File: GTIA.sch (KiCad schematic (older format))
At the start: 0 parts

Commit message: GTIA
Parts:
- added C111: 820pF, Atari:C_Axial_L5.1mm_D2.5mm_P12.50mm_Horizontal, symbol Device:C
- added C206, C59: 22pF, Atari:C_Axial_L5.1mm_D2.5mm_P12.50mm_Horizontal, symbol Device:C
- added C42, C48, C51, C58, C61: 100nF, Atari:C_Axial_L5.1mm_D2.5mm_P12.50mm_Horizontal, symbol Device:C
- added C44: 68pF, Atari:C_Axial_L5.1mm_D2.5mm_P12.50mm_Horizontal, symbol Device:C
- added C45: 220pF, Atari:C_Axial_L5.1mm_D2.5mm_P12.50mm_Horizontal, symbol Device:C
- added C46, C47, C96, C97: 1nF, Atari:C_Axial_L5.1mm_D2.5mm_P12.50mm_Horizontal, symbol Device:C
- added C50: 10uF, Capacitor_THT:CP_Radial_D8.0mm_P2.50mm, symbol Device:CP
- added C60: 560pF, Atari:C_Axial_L5.1mm_D2.5mm_P12.50mm_Horizontal, symbol Device:C
- added D2, D3, D4: 1N4148, Diode_THT:D_DO-35_SOD27_P7.62mm_Horizontal, symbol Diode:1N4148
- added FB31, FB9: Ferrite_Bead, Atari:L_Axial_L7.0mm_D3.3mm_P12.50mm_Horizontal_Fastron_MICC, symbol Device:Ferrite_Bead
- added L23, L30, L6, L66: 100uH, symbol Device:L
- added L37: Bead or 470R, symbol Device:L
- added L5: 820uH, symbol Device:L
- added L8: 1,5uH, symbol Device:L
- added Q1, Q2, Q3, Q6: 2N3904, Package_TO_SOT_THT:TO-92, symbol Transistor_BJT:2N3904
- added R116: 51, Atari:R_Axial_DIN0207_L3.6mm_D2.2mm_P10.16mm_Horizontal, symbol Device:R
- added R132, R133: 220, Atari:R_Axial_DIN0207_L3.6mm_D2.2mm_P10.16mm_Horizontal, symbol Device:R
- added R134, R135, R136, R71: 470, Atari:R_Axial_DIN0207_L3.6mm_D2.2mm_P10.16mm_Horizontal, symbol Device:R
- added R201, R69: 6k8, Atari:R_Axial_DIN0207_L3.6mm_D2.2mm_P10.16mm_Horizontal, symbol Device:R
- added R202: 180, Atari:R_Axial_DIN0207_L3.6mm_D2.2mm_P10.16mm_Horizontal, symbol Device:R
- added R204: 47, Atari:R_Axial_DIN0207_L3.6mm_D2.2mm_P10.16mm_Horizontal, symbol Device:R
- added R205: 150, Atari:R_Axial_DIN0207_L3.6mm_D2.2mm_P10.16mm_Horizontal, symbol Device:R
- added R33: 3k3, Atari:R_Axial_DIN0207_L3.6mm_D2.2mm_P10.16mm_Horizontal, symbol Device:R
- added R35: 33k, Atari:R_Axial_DIN0207_L3.6mm_D2.2mm_P10.16mm_Horizontal, symbol Device:R
- added R36: 680, Atari:R_Axial_DIN0207_L3.6mm_D2.2mm_P10.16mm_Horizontal, symbol Device:R
- added R37, R41, R42, R43, R44, R45, R72: 1k, Atari:R_Axial_DIN0207_L3.6mm_D2.2mm_P10.16mm_Horizontal, symbol Device:R
- added R46: 1k6, Atari:R_Axial_DIN0207_L3.6mm_D2.2mm_P10.16mm_Horizontal, symbol Device:R
- added R47: 36k, Atari:R_Axial_DIN0207_L3.6mm_D2.2mm_P10.16mm_Horizontal, symbol Device:R
- added R48: 18k, Atari:R_Axial_DIN0207_L3.6mm_D2.2mm_P10.16mm_Horizontal, symbol Device:R
- added R49: 9k1, Atari:R_Axial_DIN0207_L3.6mm_D2.2mm_P10.16mm_Horizontal, symbol Device:R
- added R50, R73: 4k7, Atari:R_Axial_DIN0207_L3.6mm_D2.2mm_P10.16mm_Horizontal, symbol Device:R
- added R51: 750, Atari:R_Axial_DIN0207_L3.6mm_D2.2mm_P10.16mm_Horizontal, symbol Device:R
- added R52: 2k, Atari:R_Axial_DIN0207_L3.6mm_D2.2mm_P10.16mm_Horizontal, symbol Device:R
- added R53: 100, Atari:R_Axial_DIN0207_L3.6mm_D2.2mm_P10.16mm_Horizontal, symbol Device:R
- added R70: 10k, Atari:R_Axial_DIN0207_L3.6mm_D2.2mm_P10.16mm_Horizontal, symbol Device:R
- added RV38: 500k, Potentiometer_THT:Potentiometer_ACP_CA9-V10_Vertical_Hole, symbol Device:R_POT
- added U17: GTIA, Package_DIP:DIP-40_W15.24mm_Socket, symbol Atari:GTIA
- added U18: 74LS08, Package_DIP:DIP-14_W7.62mm_Socket, symbol 74xx:74LS08
- added U20: 4050, Package_DIP:DIP-16_W7.62mm_Socket, symbol 4xxx:4050
- added U21: 74LS74, Package_DIP:DIP-14_W7.62mm_Socket, symbol 74xx:74LS74
- added Y2: 4,43 MHz, Crystal:Crystal_HC18-U_Horizontal, symbol Device:Crystal
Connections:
- new net: R134.2, U17.12 (S0)
- new net: R135.2, U17.13 (S1)
- new net: R136.2, U17.14 (S2)
- new net: Q6.3 (C), R70.1, R72.2, U17.16 (PAL)
- new net: C48.2, RV38.2, U17.17 (CADJ)
- new net: L6.2, R33.2, R41.2, U17.21 (COLOR)
- new net: R44.2, U17.22 (LUM1), U20.11
- new net: R43.2, U17.23 (LUM2), U20.5
- new net: R42.2, U17.24 (LUM3), U20.3
- new net: U17.25 (CSYNC), U20.14
- new net: C206.2, L37.1, U17.28 (OSC), U21.3 (C)
- new net: R45.2, U17.31 (LUM0), U20.7
- new net: R132.2, U17.8 (T0), U18.12
- new net: R133.2, U17.9 (T1), U18.13
- new net: C44.1, Q1.2 (B), R35.2
- new net: C45.2, Q1.3 (C), R36.2
- new net: C45.1, D2.1 (K), D3.2 (A)
- new net: C46.2, D3.1 (K), R37.2
- new net: C47.2, R37.1, RV38.1
- new net: U21.2 (D), U21.6 (~Q)
- new net: U21.11 (C), U21.5 (Q)
- new net: U21.12 (D), U21.8 (~Q)
- new net: C59.1, C60.2, R73.2, U21.9 (Q)
- new net: C58.2, U21.7 (GND)
- new net: C59.2, Y2.1
- new net: C111.1, L8.1, R71.2, Y2.2
- new net: Q6.2 (B), R69.1, R70.2, R71.1
- new net: C111.2, C61.2, L8.2
- new net: R50.2, U20.2
- new net: R49.2, U20.4
- new net: R47.2, U20.6
- new net: R48.2, U20.12
- new net: D4.1 (K), U20.15
- new net: C50.1, C51.1, L5.1, R116.1, R46.1, U20.1 (VCC)
- new net: Q3.2 (B), R46.2, R47.1, R48.1, R49.1, R50.1, R51.1, R52.1
- new net: D4.2 (A), R51.2
- new net: Q3.1 (E), R204.2, R53.1
- new net: Q3.3 (C), R116.2
- new net: FB9.2, R204.1
- new net: L66.2, R33.1
- new net: Q2.2 (B), R201.1
- new net: L6.1, R201.2
- new net: Q2.1 (E), R202.2, R205.2
- new net: FB31.2, R205.1
- new net: C97.2, L30.2, R132.1
- new net: C96.2, L23.2, R133.1
- new net +5C: Q2.3 (C)
- new net +5VA: C42.1, C58.1, D2.2 (A), L5.2, R35.1, R36.1, R41.1, R42.1, R43.1, R44.1, R45.1, R72.1, R73.1, U17.27 (VCC), U21.1 (~R), U21.10 (~S), U21.13 (~R), U21.14 (VCC), U21.4 (~S)
- new net A0: U17.2 (A0)
- new net A1: U17.1 (A1)
- new net A2: U17.40 (A2)
- new net A3: U17.39 (A3)
- new net A4: U17.38 (A4)
- new net AN0: U17.18 (AN0)
- new net AN1: U17.19 (AN1)
- new net AN2: U17.20 (AN2)
- new net BELL: U17.15 (S3)
- new net CHROMA: FB31.1
- new net COLOR: L66.1
- new net D0: U17.7 (D0)
- new net D1: U17.6 (D1)
- new net D2: U17.5 (D2)
- new net D3: U17.4 (D3)
- new net D4: U17.37 (D4)
- new net D5: U17.36 (D5)
- new net D6: U17.35 (D6)
- new net D7: U17.34 (D7)
- new net FO0: U17.29 (FO0)
- new net GND: C206.1, C42.2, C46.1, C47.1, C48.1, C50.2, C51.2, C60.1, C61.1, C96.1, C97.1, Q1.1 (E), Q6.1 (E), R202.1, R52.2, R53.2, R69.2, RV38.3, U17.3 (VSS), U20.8 (VSS), U20.9
- new net GTIA: U17.32 (~CS)
- new net HALT: U17.26 (HALT)
- new net LP: U18.11
- new net MONO: FB9.1
- new net O1: C44.2
- new net O2: U17.30 (O2)
- new net OPTION: R136.1
- new net OSC: L37.2
- new net RD5: U17.11 (T3)
- new net RW: U17.33 (R/~W)
- new net SELECT: R135.1
- new net START: R134.1
- new net TRIG0: L30.1
- new net TRIG1: L23.1
- no-connect marks 0 -> 1
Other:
- note added: "When L=470R\nC206 is not mounted"

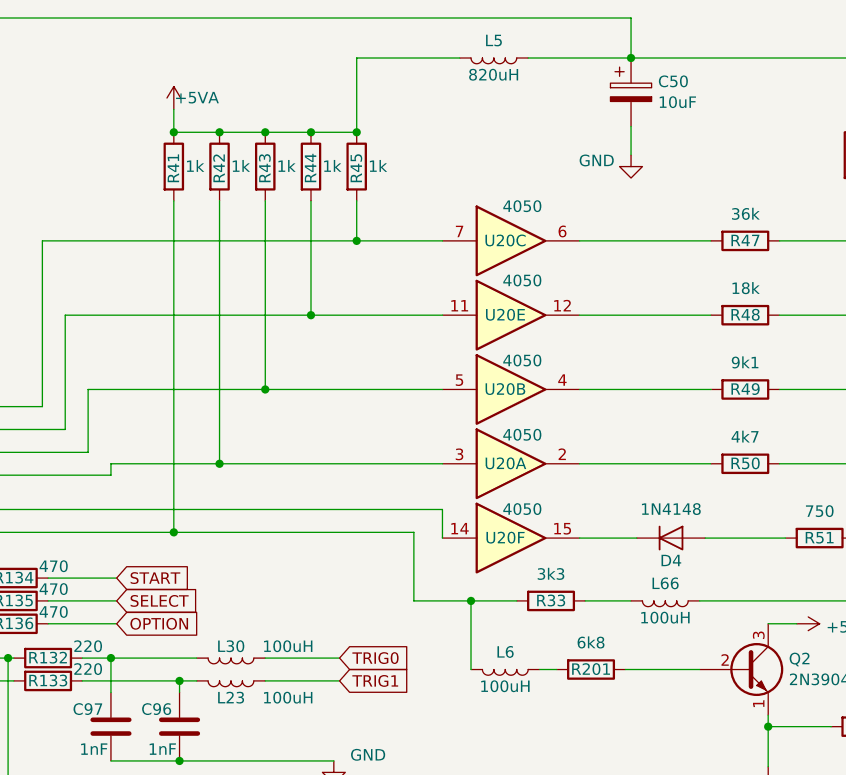
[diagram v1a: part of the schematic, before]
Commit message: GTIA put on board
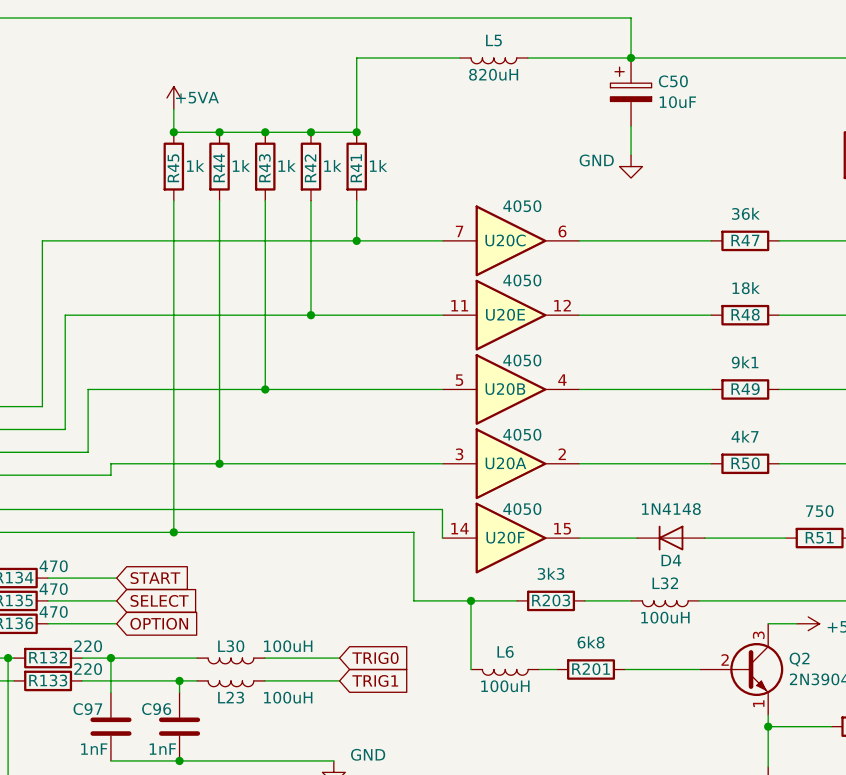
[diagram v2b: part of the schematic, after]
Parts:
- C50: footprint Capacitor_THT:CP_Radial_D8.0mm_P2.50mm -> Capacitor_THT:CP_Radial_D5.0mm_P2.00mm
- D4: footprint Diode_THT:D_DO-35_SOD27_P7.62mm_Horizontal -> Diode_THT:D_DO-35_SOD27_P12.70mm_Horizontal
- L23, L30, L37, L5, L6, L8: footprint (none) -> Atari:L_Axial_L7.0mm_D3.3mm_P12.50mm_Horizontal_Fastron_MICC
- L32: renamed from L66; footprint (none) -> Atari:L_Axial_L7.0mm_D3.3mm_P12.50mm_Horizontal_Fastron_MICC
- renumbered R33 to R203
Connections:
- net at L6.2, R203.2, U17.21 (COLOR): now also R45.2; no longer R41.2
- net at U17.22 (LUM1), U20.11: now also R42.2; no longer R44.2
- net at U17.24 (LUM3), U20.3: now also R44.2; no longer R42.2
- net at U17.31 (LUM0), U20.7: now also R41.2; no longer R45.2
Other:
- moved on the sheet: R41, R42, R44, R45

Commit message: MMU, Joy, Cart and Video
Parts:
- added J2: Video, Atari:DIN_5_pin, symbol Connector:DIN-5_180degree
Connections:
- net +5VA: no longer R72.1, R73.1
- net CHROMA: now also J2.5
- net GND: now also J2.2
- net MONO: now also J2.1
- new net +5V: R72.1, R73.1
- new net AUDIO: J2.3
- new net COMPOSITE: J2.4
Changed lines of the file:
@@
 $Descr A4 11693 8268
 encoding utf-8
-Sheet 9 14
+Sheet 9 15
 Title ""
 Date ""
@@
 $EndComp
 $Comp
-L power:+5VA #PWR0163
-U 1 1 602A10C2
-P 7275 4700
-F 0 "#PWR0163" H 7275 4550 50  0001 C CNN
-F 1 "+5VA" H 7290 4873 50  0000 C CNN
-F 2 "" H 7275 4700 50  0001 C CNN
-F 3 "" H 7275 4700 50  0001 C CNN
-	1    7275 4700
-	1    0    0    -1
-$EndComp
-$Comp
 L Device:Crystal Y2
 U 1 1 602A36C7
@@
 	5600 4425 9375 4425
 Connection ~ 9375 4425
-$Comp
-L power:+5VA #PWR0166
-U 1 1 602BC276
-P 10050 4350
-F 0 "#PWR0166" H 10050 4200 50  0001 C CNN
-F 1 "+5VA" H 10065 4523 50  0000 C CNN
-F 2 "" H 10050 4350 50  0001 C CNN
-F 3 "" H 10050 4350 50  0001 C CNN
-	1    10050 4350
-	1    0    0    -1
-$EndComp
 Wire Wire Line
 	9925 4425 10050 4425
@@
 Wire Wire Line
 	1050 525  1050 1600
+$Comp
+L Connector:DIN-5_180degree J2
+U 1 1 6027E470
+P 4525 7150
+F 0 "J2" H 4525 7150 50  0000 C CNN
+F 1 "Video" H 4525 6875 50  0000 C CNN
+F 2 "Atari:DIN_5_pin" H 4525 7150 50  0001 C CNN
+F 3 "http://www.mouser.com/ds/2/18/40_c091_abd_e-75918.pdf" H 4525 7150 50  0001 C CNN
+	1    4525 7150
+	-1   0    0    1
+$EndComp
+$Comp
+L power:GND #PWR0182
+U 1 1 6029DB7D
+P 4525 7525
+F 0 "#PWR0182" H 4525 7275 50  0001 C CNN
+F 1 "GND" H 4530 7352 50  0000 C CNN
+F 2 "" H 4525 7525 50  0001 C CNN
+F 3 "" H 4525 7525 50  0001 C CNN
+	1    4525 7525
+	1    0    0    -1
+$EndComp
+Wire Wire Line
+	4525 7450 4525 7525
+Text GLabel 4225 7250 0    50   Input ~ 0
+CHROMA
+Text GLabel 4225 7150 0    50   Input ~ 0
+AUDIO
+Text GLabel 4825 7250 2    50   Input ~ 0
+COMPOSITE
+Text GLabel 4825 7150 2    50   Input ~ 0
+MONO
+$Comp
+L power:+5V #PWR0163
+U 1 1 602CA007
+P 10050 4350
+F 0 "#PWR0163" H 10050 4200 50  0001 C CNN
+F 1 "+5V" H 10065 4523 50  0000 C CNN
+F 2 "" H 10050 4350 50  0001 C CNN
+F 3 "" H 10050 4350 50  0001 C CNN
+	1    10050 4350
+	1    0    0    -1
+$EndComp
+$Comp
+L power:+5V #PWR0166
+U 1 1 602CB043
+P 7275 4700
+F 0 "#PWR0166" H 7275 4550 50  0001 C CNN
+F 1 "+5V" H 7290 4873 50  0000 C CNN
+F 2 "" H 7275 4700 50  0001 C CNN
+F 3 "" H 7275 4700 50  0001 C CNN
+	1    7275 4700
+	1    0    0    -1
+$EndComp
 $EndSCHEMATC

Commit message: Put elements on board
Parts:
- D2, D3: footprint Diode_THT:D_DO-35_SOD27_P7.62mm_Horizontal -> Diode_THT:D_DO-35_SOD27_P12.70mm_Horizontal
- Q1, Q2, Q3: footprint Package_TO_SOT_THT:TO-92 -> Package_TO_SOT_THT:TO-92L_Wide
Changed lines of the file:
@@
 F 0 "Q1" H 1690 6246 50  0000 L CNN
 F 1 "2N3904" H 1690 6155 50  0000 L CNN
-F 2 "Package_TO_SOT_THT:TO-92" H 1700 6125 50  0001 L CIN
+F 2 "Package_TO_SOT_THT:TO-92L_Wide" H 1700 6125 50  0001 L CIN
 F 3 "https://www.fairchildsemi.com/datasheets/2N/2N3904.pdf" H 1500 6200 50  0001 L CNN
 	1    1500 6200
@@
 F 0 "D2" V 2450 5825 50  0000 R CNN
 F 1 "1N4148" V 2450 5600 50  0000 R CNN
-F 2 "Diode_THT:D_DO-35_SOD27_P7.62mm_Horizontal" H 2375 5500 50  0001 C CNN
+F 2 "Diode_THT:D_DO-35_SOD27_P12.70mm_Horizontal" H 2375 5500 50  0001 C CNN
 F 3 "https://assets.nexperia.com/documents/data-sheet/1N4148_1N4448.pdf" H 2375 5675 50  0001 C CNN
 	1    2375 5675
@@
 F 0 "D3" H 2550 5950 50  0000 C CNN
 F 1 "1N4148" H 2675 5875 50  0000 C CNN
-F 2 "Diode_THT:D_DO-35_SOD27_P7.62mm_Horizontal" H 2675 5825 50  0001 C CNN
+F 2 "Diode_THT:D_DO-35_SOD27_P12.70mm_Horizontal" H 2675 5825 50  0001 C CNN
 F 3 "https://assets.nexperia.com/documents/data-sheet/1N4148_1N4448.pdf" H 2675 6000 50  0001 C CNN
 	1    2675 6000
@@
 F 0 "Q3" H 9390 1671 50  0000 L CNN
 F 1 "2N3904" H 9390 1580 50  0000 L CNN
-F 2 "Package_TO_SOT_THT:TO-92" H 9400 1550 50  0001 L CIN
+F 2 "Package_TO_SOT_THT:TO-92L_Wide" H 9400 1550 50  0001 L CIN
 F 3 "https://www.fairchildsemi.com/datasheets/2N/2N3904.pdf" H 9200 1625 50  0001 L CNN
 	1    9200 1625
@@
 F 0 "Q2" H 8115 3421 50  0000 L CNN
 F 1 "2N3904" H 8115 3330 50  0000 L CNN
-F 2 "Package_TO_SOT_THT:TO-92" H 8125 3300 50  0001 L CIN
+F 2 "Package_TO_SOT_THT:TO-92L_Wide" H 8125 3300 50  0001 L CIN
 F 3 "https://www.fairchildsemi.com/datasheets/2N/2N3904.pdf" H 7925 3375 50  0001 L CNN
 	1    7925 3375
